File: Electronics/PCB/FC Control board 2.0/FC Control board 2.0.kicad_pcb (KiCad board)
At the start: 2 copper layers, 53.2 x 98.4 mm, 78 parts, among them IC1 A3909GLNTR-T, IC2 A3909GLNTR-T, J1 USB_C_Receptacle_USB2.0, J2 CAM, J3 Servo, J4 Hall-M1, J5 Hall-M2, J6 Hall-M0, J7 Hall-M3, M0 Motor_DC_ALT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

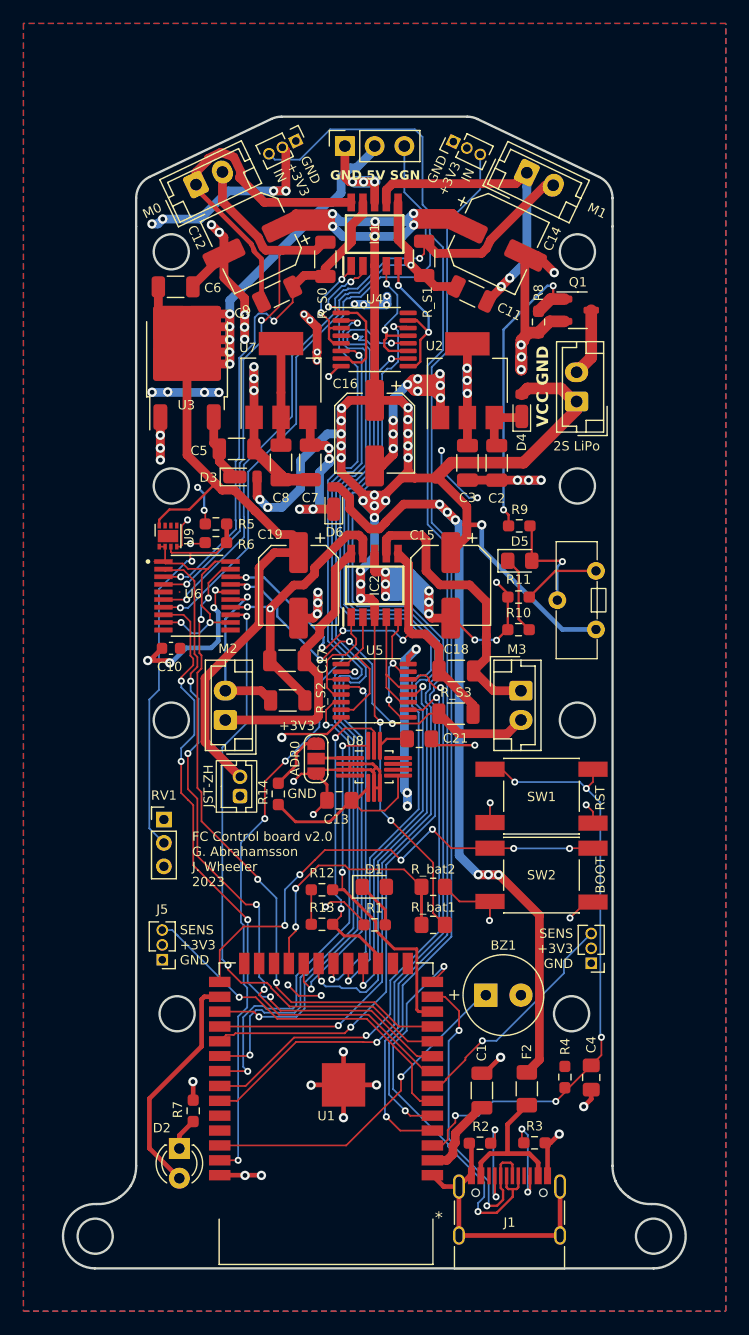
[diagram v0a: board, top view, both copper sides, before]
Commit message: Add clamping diodes and opto couplers
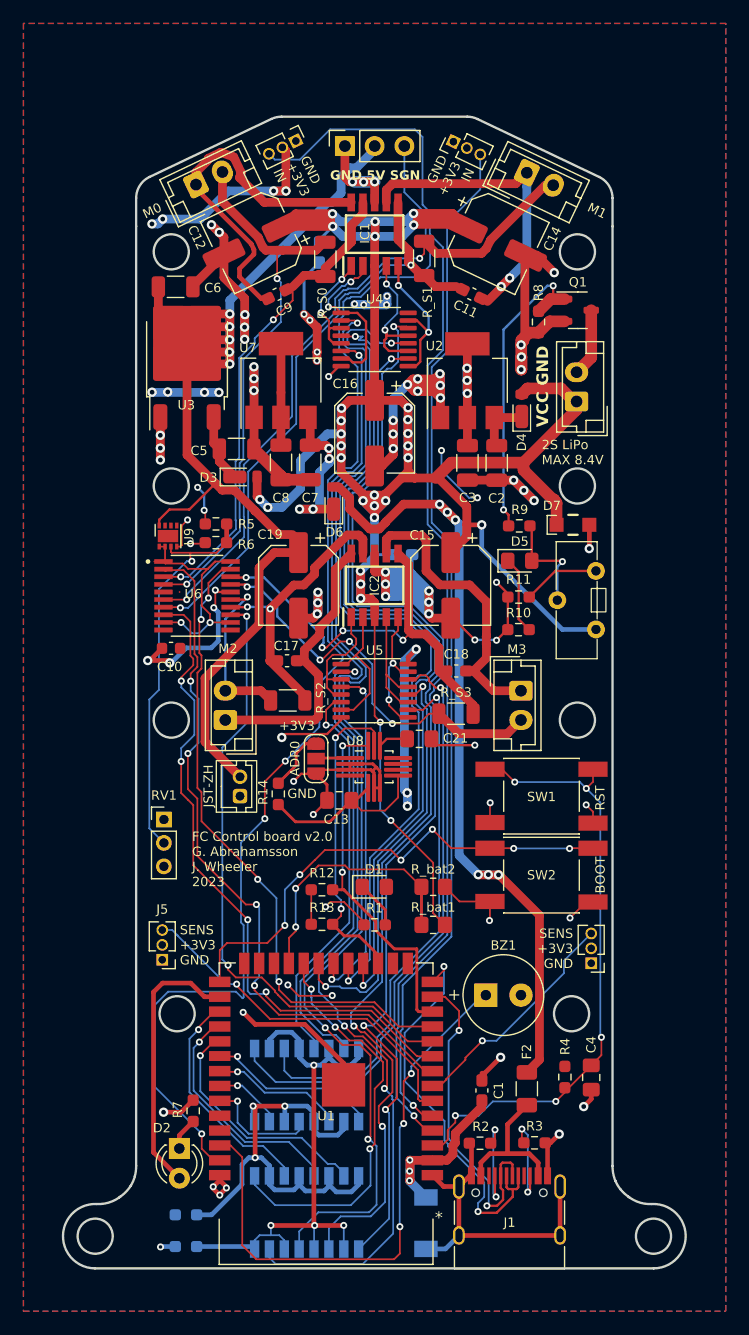
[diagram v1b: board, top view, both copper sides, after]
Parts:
- added C20: 100n, Capacitor_SMD:C_0603_1608Metric_Pad1.08x0.95mm_HandSolder, B.Cu at (209.0, 137.1)
- added C22: 100n, Capacitor_SMD:C_0603_1608Metric_Pad1.08x0.95mm_HandSolder, B.Cu at (201.9, 111.3)
- added D7: HPZRC8V8QX, FC_footprint_library:HPZRC8V8QX, F.Cu at (223.6, 134.5)
- added D8: PDZVTR36B, FC_footprint_library:PDZVTR36B, B.Cu at (211.0, 194.2)
- added IC3: LTV-247, KiCad:LTV247, B.Cu at (200.8, 193.3)
- added IC4: LTV-247, KiCad:LTV247, B.Cu at (200.8, 182.4)
- added R15: R_PWM, Resistor_SMD:R_0603_1608Metric_Pad0.98x0.95mm_HandSolder, B.Cu at (190.5, 193.5)
- added R16: R_OPTO, Resistor_SMD:R_0603_1608Metric_Pad0.98x0.95mm_HandSolder, B.Cu at (190.5, 196.2)
- C1: value C -> 100n; footprint Capacitor_SMD:C_1206_3216Metric -> Capacitor_SMD:C_0603_1608Metric_Pad1.08x0.95mm_HandSolder
- C11, C17, C18, C9: value C_MAYBE -> 100n; footprint Capacitor_SMD:C_1206_3216Metric -> Capacitor_SMD:C_0603_1608Metric_Pad1.08x0.95mm_HandSolder
- moved G*** 23.8 mm to (206.9, 168.0)
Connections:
- U4 pad 10: /FWR_1 -> /OPTO_FWR_1
- U4 pad 14: /REV_1 -> /OPTO_REV_1
- U4 pad 2: /FWR_0 -> /OPTO_FWR_0
- U4 pad 6: /REV_0 -> /OPTO_REV_0
- U5 pad 10: /FWR_3 -> /OPTO_FWR_3
- U5 pad 14: /REV_3 -> /OPTO_REV_3
- U5 pad 2: /FWR_2 -> /OPTO_FWR_2
- U5 pad 6: /REV_2 -> /OPTO_REV_2
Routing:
- net /OPTO_FWR_0: track 0.00 -> 104.1 mm, vias 0 -> 3
- net /OPTO_FWR_1: track 0.00 -> 94.9 mm, vias 0 -> 3
- net /OPTO_REV_1: track 0.00 -> 94.8 mm, vias 0 -> 3
- net /OPTO_REV_0: track 0.00 -> 94.4 mm, vias 0 -> 3
- net /REV_1: track 84.7 -> 20.6 mm, vias 2 -> 1
- net /FWR_1: track 80.4 -> 20.4 mm, vias 2 -> 1
- net /REV_0: track 72.4 -> 19.7 mm, vias 2 -> 1
- net /OPTO_REV_3: track 0.00 -> 50.9 mm, vias 0 -> 1
- net /OPTO_3V3: track 0.00 -> 47.3 mm, vias 0 -> 4
- net /OPTO_FWR_3: track 0.00 -> 46.7 mm, vias 0 -> 1
- net /FWR_3: track 48.8 -> 5.97 mm, vias 2 -> 1
- net /REV_3: track 51.7 -> 9.89 mm, vias 2 -> 1
- net /OPTO_GND: track 0.00 -> 40.9 mm, vias 0 -> 3
- net /OPTO_FWR_2: track 0.00 -> 39.6 mm, vias 0 -> 1
- net /FWR_0: track 70.1 -> 35.1 mm, vias 2 -> 3
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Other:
- board text added: "2S LiPo MAX 8.4V"
- board text removed: "2S LiPo"

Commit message: Final version of 2.0 [Ordered]
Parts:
- D7: moved to B.Cu
- U9: footprint Package_DFN_QFN:DFN-8-1EP_2x2mm_P0.5mm_EP1.05x1.75mm -> Package_SO:SOIC-8-1EP_3.9x4.9mm_P1.27mm_EP2.514x3.2mm; moved to B.Cu
- moved D7 24.8 mm to (198.9, 136.5), turned to -90 degrees
- moved U9 1.63 mm to (190.6, 135.8), turned to 180 degrees
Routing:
- net GNDREF: track 296.4 -> 302.6 mm, vias 73 -> 75
- net Net-(U6-REF1): track 21.4 -> 26.1 mm, vias 2 -> 3
- net VCC: track 225.9 -> 221.8 mm
- net +3V3: track 108.5 -> 105.1 mm, vias 26 -> 24
- net /in+0: track 48.0 -> 51.1 mm
- net /in-0: track 41.4 -> 44.5 mm
- net /in-1: track 51.5 -> 54.5 mm
- net /in+1: track 57.3 -> 59.9 mm
- net +5V: track 98.1 -> 97.9 mm, vias 5 -> 6
